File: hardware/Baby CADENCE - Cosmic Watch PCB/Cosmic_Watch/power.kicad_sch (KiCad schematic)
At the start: 2 parts, among them J1 USB_B_Micro, U3 LT3461ES6-TRPBF

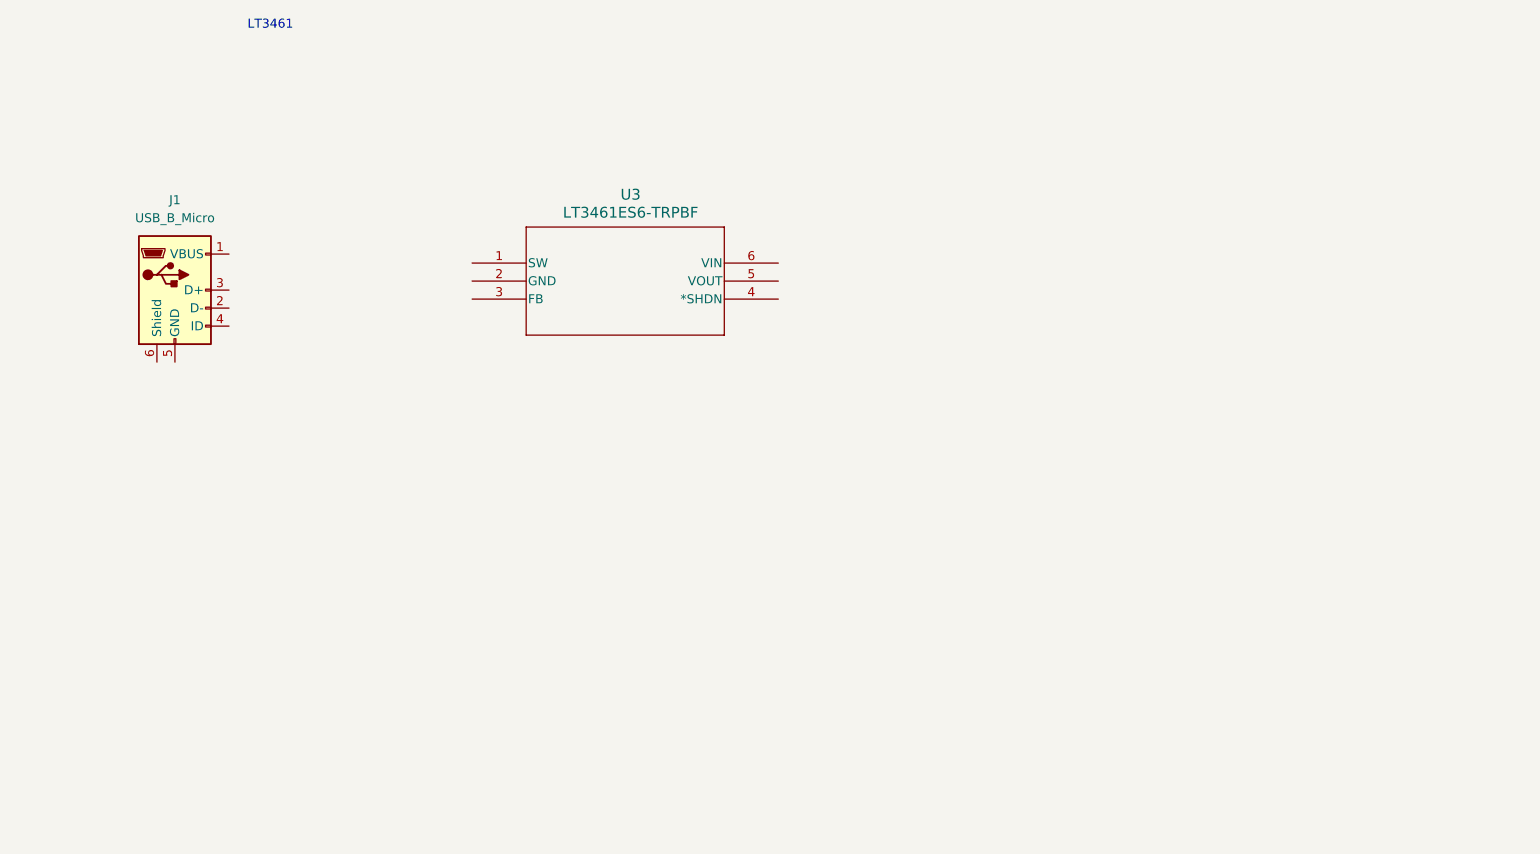
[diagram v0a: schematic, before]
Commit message: More Updates
Almost done with power.sch, just need to figure out ferrite bead values/other manufacturers since the old one is obsolete. Still figuring out values for the amplification stage.
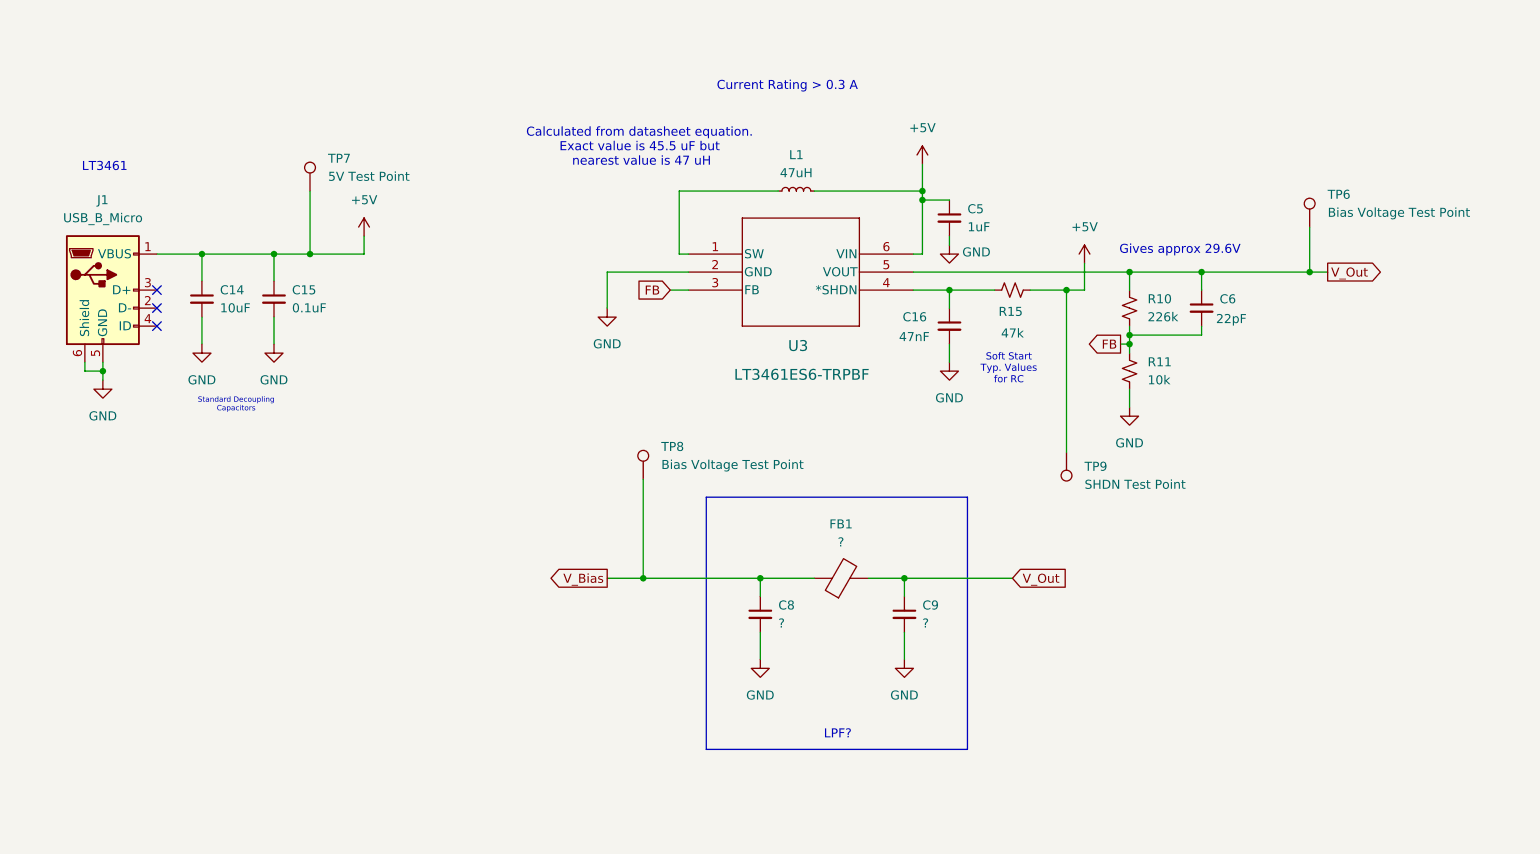
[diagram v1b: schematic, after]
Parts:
- added C14: 10uF, symbol Device:C_Small
- added C15: 0.1uF, symbol Device:C_Small
- added C16: 47nF, symbol Device:C_Small
- added C5: 1uF, symbol Device:C_Small
- added C6: 22pF, symbol Device:C_Small
- added C8, C9: ?, symbol Device:C_Small
- added FB1: ?, symbol Device:FerriteBead
- added L1: 47uH, symbol Device:L_Small
- added R10: 226k, symbol Device:R_Small_US
- added R11: 10k, symbol Device:R_Small_US
- added R15: 47k, symbol Device:R_Small_US
- added TP6, TP8: Bias Voltage Test Point, symbol Connector:TestPoint
- added TP7: 5V Test Point, symbol Connector:TestPoint
- added TP9: SHDN Test Point, symbol Connector:TestPoint
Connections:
- net at U3.1 (SW): now also L1.1
- net GND: now reaches U3.2 (GND)
- net GND: now also J1.5 (GND), J1.6 (Shield), C14.2, C15.2, C16.2, C5.2, C8.2, C9.2, R11.2
- net FB: now reaches U3.3 (FB)
- net FB: now also C6.2, R10.2, R11.1
- net at U3.4 (*SHDN): now also C16.1, R15.1
- net V_Out: now reaches U3.5 (VOUT)
- net V_Out: now also C6.1, C9.1, FB1.2, R10.1, TP6.1
- net +5V: now reaches U3.6 (VIN)
- net +5V: now also J1.1 (VBUS), C14.1, C15.1, C5.1, L1.2, R15.2, TP7.1, TP9.1
- new net V_Bias: C8.1, FB1.1, TP8.1
- no-connect marks 0 -> 3
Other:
- note added: "Calculated from datasheet equation. Exact value is 45.5 uF but nearest value is 47 uH"
- note added: "Current Rating > 0.3 A"
- note added: "Gives approx 29.6V"
- note added: "LPF?"
- note added: "Soft Start Typ. Values for RC"
- note added: "Standard Decoupling Capacitors"
- moved on the sheet: J1, U3

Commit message: Updates
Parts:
- added TP10: Output Voltage Test Point, symbol Connector:TestPoint
- C8: value ? -> 1uF
- C9: value ? -> 0.47uF
- FB1: value ? -> 2.5kohm
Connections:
- net V_Out: now also TP10.1
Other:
- moved on the sheet: C8, C9, FB1, TP8

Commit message: Added 5V Coax Connection
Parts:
- removed TP6: Bias Voltage Test Point, symbol Connector:TestPoint
- added J4: Conn_Coaxial, symbol Connector:Conn_Coaxial
- renumbered TP7 to TP6, TP8 to TP7, TP10 to TP8
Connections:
- net +5V: now also J4.1 (In)
- net GND: now also J4.2 (Ext)
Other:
- note added: "From the Payload Computer"
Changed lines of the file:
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@@
+		)
+	)
+	(text "From the Payload Computer\n"
+		(exclude_from_sim no)
+		(at 48.006 136.652 0)
+		(effects
+			(font
+				(size 1.27 1.27)
+			)
 		)
 	)
@@
 		(color 0 0 0 0)
 	)
-	(junction
-		(at 209.55 97.79)
-		(diameter 0)
-		(color 0 0 0 0)
-	)
 	(no_connect
 		(at 46.99 100.33)
@@
 	(wire
 		(pts
+			(xy 40.64 152.4) (xy 40.64 149.86)
+		)
+		(stroke
+			(width 0)
+			(type default)
+		)
+	)
+	(wire
+		(pts
 			(xy 137.16 139.7) (xy 137.16 153.67)
 		)
@@
 	(wire
 		(pts
-			(xy 194.31 97.79) (xy 209.55 97.79)
-		)
-		(stroke
-			(width 0)
-			(type default)
-		)
-	)
-	(wire
-		(pts
 			(xy 53.34 95.25) (xy 53.34 99.06)
 		)
@@
 	(wire
 		(pts
+			(xy 29.21 144.78) (xy 35.56 144.78)
+		)
+		(stroke
+			(width 0)
+			(type default)
+		)
+	)
+	(wire
+		(pts
 			(xy 39.37 110.49) (xy 39.37 111.76)
 		)
@@
 	(wire
 		(pts
-			(xy 209.55 91.44) (xy 209.55 97.79)
-		)
-		(stroke
-			(width 0)
-			(type default)
-		)
-	)
-	(wire
-		(pts
 			(xy 177.8 100.33) (xy 177.8 96.52)
 		)
@@
 	(wire
 		(pts
-			(xy 209.55 97.79) (xy 212.09 97.79)
+			(xy 194.31 97.79) (xy 212.09 97.79)
 		)
 		(stroke
@@
 		(dnp no)
 		(fields_autoplaced yes)
-		(property "Reference" "TP10"
+		(property "Reference" "TP8"
 			(at 139.7 135.1279 0)
 			(effects
@@
 			(project "Cosmic_Watch"
 				(path "/901a4a81-3d4a-4d59-b0fc-ea1dade1210f/94b942db-2822-486c-90f4-c726bdd9ff86"
-					(reference "TP10")
+					(reference "TP8")
 					(unit 1)
 				)
@@
 	)
 	(symbol
+		(lib_id "power:GND")
+		(at 40.64 152.4 0)
+		(unit 1)
+		(exclude_from_sim no)
+		(in_bom yes)
+		(on_board yes)
+		(dnp no)
+		(fields_autoplaced yes)
+		(property "Reference" "#PWR033"
+			(at 40.64 158.75 0)
+			(effects
+				(font
+					(size 1.27 1.27)
+				)
+				(hide yes)
+			)
+		)
+		(property "Value" "GND"
+			(at 40.64 157.48 0)
+			(effects
+				(font
+					(size 1.27 1.27)
+				)
+			)
+		)
+		(property "Footprint" ""
+			(at 40.64 152.4 0)
+			(effects
+				(font
+					(size 1.27 1.27)
+				)
+				(hide yes)
+			)
+		)
+		(property "Datasheet" ""
+			(at 40.64 152.4 0)
+			(effects
+				(font
+					(size 1.27 1.27)
+				)
+				(hide yes)
+			)
+		)
+		(property "Description" "Power symbol creates a global label with name \"GND\" , ground"
+			(at 40.64 152.4 0)
+			(effects
+				(font
+					(size 1.27 1.27)
+				)
+				(hide yes)
+			)
+		)
+		(pin "1"
+		)
+		(instances
+			(project "Cosmic_Watch"
+				(path "/901a4a81-3d4a-4d59-b0fc-ea1dade1210f/94b942db-2822-486c-90f4-c726bdd9ff86"
+					(reference "#PWR033")
+					(unit 1)
+				)
+			)
+		)
+	)
+	(symbol
 		(lib_id "Device:C_Small")
 		(at 116.84 158.75 0)
@@
 	)
 	(symbol
-		(lib_id "Connector:TestPoint")
-		(at 209.55 91.44 0)
-		(unit 1)
-		(exclude_from_sim no)
-		(in_bom yes)
-		(on_board yes)
-		(dnp no)
-		(fields_autoplaced yes)
-		(property "Reference" "TP6"
-			(at 212.09 86.8679 0)
+		(lib_id "Connector:Conn_Coaxial")
+		(at 40.64 144.78 0)
+		(unit 1)
+		(exclude_from_sim no)
+		(in_bom yes)
+		(on_board yes)
+		(dnp no)
+		(fields_autoplaced yes)
+		(property "Reference" "J4"
+			(at 44.45 143.8031 0)
 			(effects
 				(font
@@
 			)
 		)
-		(property "Value" "Bias Voltage Test Point"
-			(at 212.09 89.4079 0)
+		(property "Value" "Conn_Coaxial"
+			(at 44.45 146.3431 0)
 			(effects
 				(font
@@
 		)
 		(property "Footprint" ""
-			(at 214.63 91.44 0)
+			(at 40.64 144.78 0)
 			(effects
 				(font
@@
 		)
 		(property "Datasheet" "~"
-			(at 214.63 91.44 0)
-			(effects
-				(font
-					(size 1.27 1.27)
-				)
-				(hide yes)
-			)
-		)
-		(property "Description" "test point"
-			(at 209.55 91.44 0)
-			(effects
-				(font
-					(size 1.27 1.27)
-				)
-				(hide yes)
-			)
-		)
-		(pin "1"
-		)
-		(instances
-			(project ""
-				(path "/901a4a81-3d4a-4d59-b0fc-ea1dade1210f/94b942db-2822-486c-90f4-c726bdd9ff86"
-					(reference "TP6")
+			(at 40.64 144.78 0)
+			(effects
+				(font
+					(size 1.27 1.27)
+				)
+				(hide yes)
+			)
+		)
+		(property "Description" "coaxial connector (BNC, SMA, SMB, SMC, Cinch/RCA, LEMO, ...)"
+			(at 40.64 144.78 0)
+			(effects
+				(font
+					(size 1.27 1.27)
+				)
+				(hide yes)
+			)
+		)
+		(pin "1"
+		)
+		(pin "2"
+		)
+		(instances
+			(project "Cosmic_Watch"
+				(path "/901a4a81-3d4a-4d59-b0fc-ea1dade1210f/94b942db-2822-486c-90f4-c726bdd9ff86"
+					(reference "J4")
 					(unit 1)
 				)
@@
 	(symbol
 		(lib_id "power:+5V")
+		(at 29.21 144.78 0)
+		(unit 1)
+		(exclude_from_sim no)
+		(in_bom yes)
+		(on_board yes)
+		(dnp no)
+		(fields_autoplaced yes)
+		(property "Reference" "#PWR02"
+			(at 29.21 148.59 0)
+			(effects
+				(font
+					(size 1.27 1.27)
+				)
+				(hide yes)
+			)
+		)
+		(property "Value" "+5V"
+			(at 29.21 139.7 0)
+			(effects
+				(font
+					(size 1.27 1.27)
+				)
+			)
+		)
+		(property "Footprint" ""
+			(at 29.21 144.78 0)
+			(effects
+				(font
+					(size 1.27 1.27)
+				)
+				(hide yes)
+			)
+		)
+		(property "Datasheet" ""
+			(at 29.21 144.78 0)
+			(effects
+				(font
+					(size 1.27 1.27)
+				)
+				(hide yes)
+			)
+		)
+		(property "Description" "Power symbol creates a global label with name \"+5V\""
+			(at 29.21 144.78 0)
+			(effects
+				(font
+					(size 1.27 1.27)
+				)
+				(hide yes)
+			)
+		)
+		(pin "1"
+		)
+		(instances
+			(project ""
+				(path "/901a4a81-3d4a-4d59-b0fc-ea1dade1210f/94b942db-2822-486c-90f4-c726bdd9ff86"
+					(reference "#PWR02")
+					(unit 1)
+				)
+			)
+		)
+	)
+	(symbol
+		(lib_id "power:+5V")
 		(at 76.2 92.71 0)
 		(unit 1)
@@
 		(dnp no)
 		(fields_autoplaced yes)
-		(property "Reference" "TP8"
+		(property "Reference" "TP7"
 			(at 82.55 135.1279 0)
 			(effects
@@
 			(project "Cosmic_Watch"
 				(path "/901a4a81-3d4a-4d59-b0fc-ea1dade1210f/94b942db-2822-486c-90f4-c726bdd9ff86"
-					(reference "TP8")
+					(reference "TP7")
 					(unit 1)
 				)
@@
 		(dnp no)
 		(fields_autoplaced yes)
-		(property "Reference" "TP7"
+		(property "Reference" "TP6"
 			(at 71.12 81.7879 0)
 			(effects
@@
 			(project "Cosmic_Watch"
 				(path "/901a4a81-3d4a-4d59-b0fc-ea1dade1210f/94b942db-2822-486c-90f4-c726bdd9ff86"
-					(reference "TP7")
-					(unit 1)
-				)
+					(reference "TP6")
+					(unit 1)
+				)
